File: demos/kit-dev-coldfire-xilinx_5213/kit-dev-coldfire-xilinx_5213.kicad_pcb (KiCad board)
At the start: 4 copper layers, 157.5 x 91.4 mm, 160 parts, among them J201 JACK_2P, P301 CONN_6, P302 CONN_2X2, P303 CONN_20X2, Q101 3906, SW201 SW_PUSH, SW202 SW_PUSH, U101 74AHC1G14, U102 MCF5213-LQFP100, U201 74HC125, U202 MAX202, U203 MAX202, U204 MAX202, U205 PCA82C251, U301 XCR3256-TQ144, Y101 8MHz

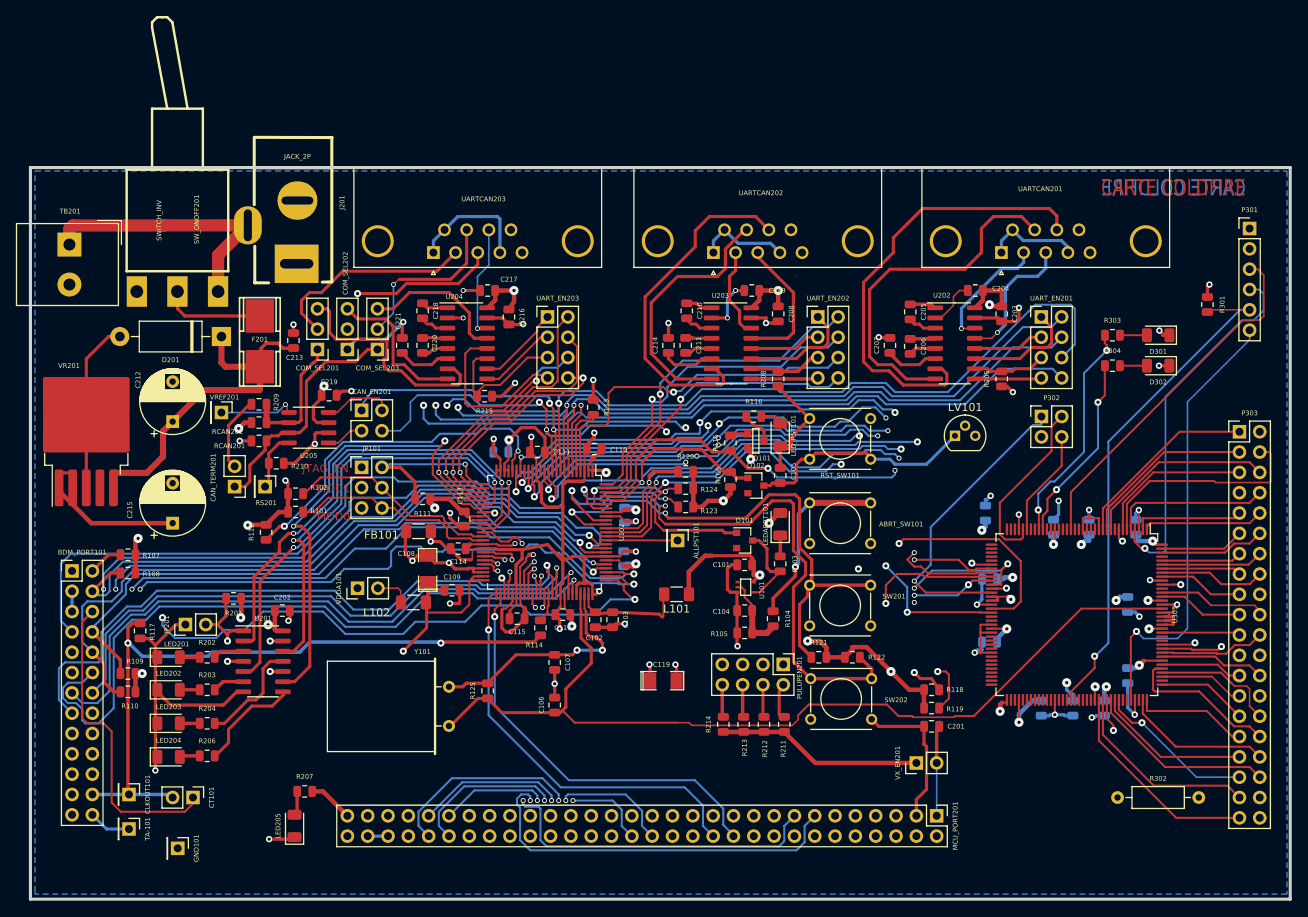
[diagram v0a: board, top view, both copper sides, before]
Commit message: feat: update kicad to 9.0.0+dfsg-1
Signed-off-by: lhdjply <lhdjply@126.com>
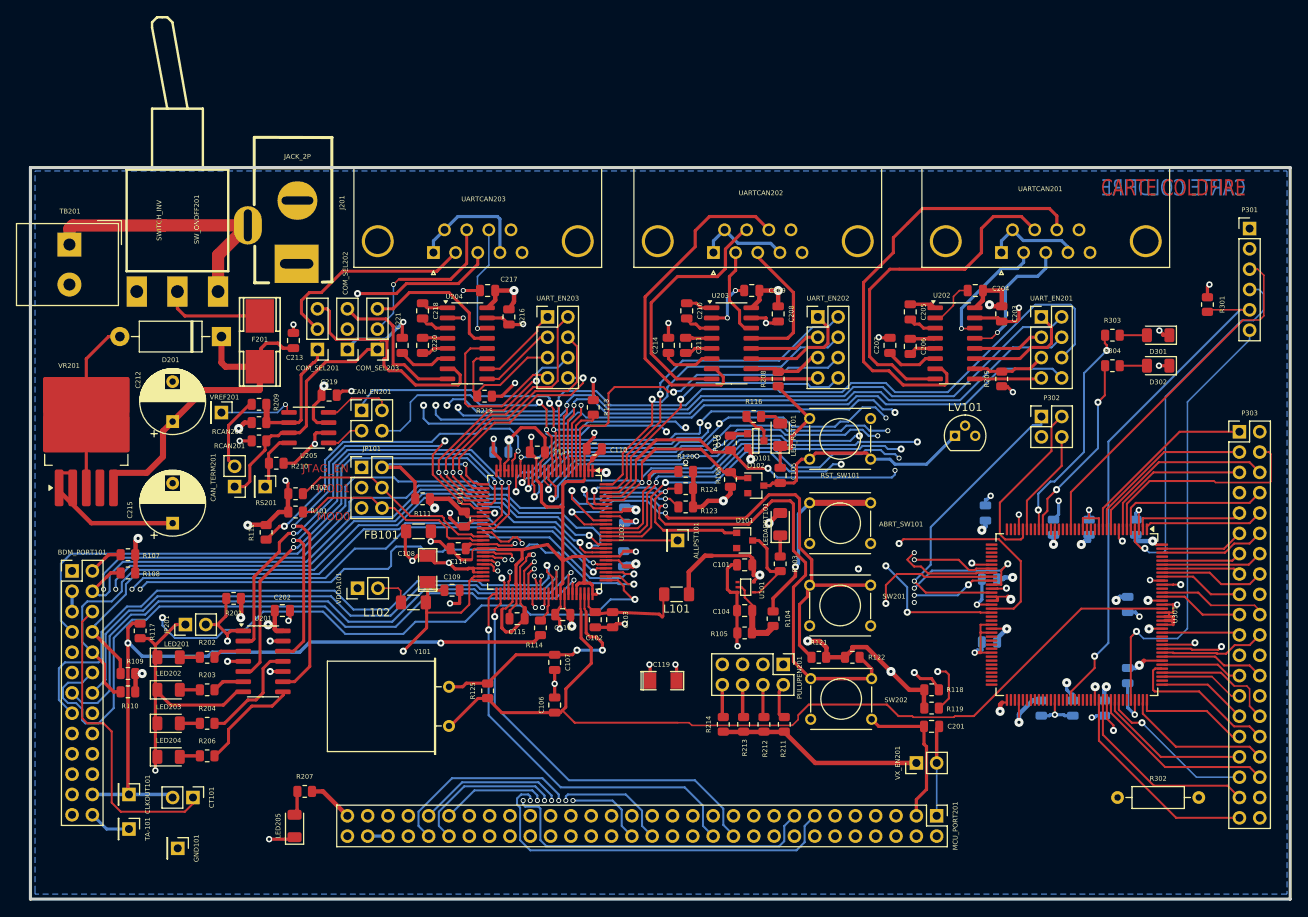
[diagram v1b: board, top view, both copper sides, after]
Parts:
- ALLPST101, CLKOUT101, GND101, RS201, TA-101, VREF201: footprint Connector_PinHeader_2.54mm:PinHeader_1x01_P2.54mm_Vertical -> kit-dev-coldfire:PinHeader_1x01_P2.54mm_Vertical
- BDM_PORT101: footprint Connector_PinHeader_2.54mm:PinHeader_2x13_P2.54mm_Vertical -> kit-dev-coldfire:PinHeader_2x13_P2.54mm_Vertical
- C101, C102, C103, C104, C105, C106, C107, C109, C110, C111, C112, C113, C114, C115, C116, C117, C118, C201, C202, C203, C204, C205, C206, C207, C208, C209, C210, C211, C213, C214, C216, C217, C218, C219, C220, C221, C301, C302, C303, C304, C305, C306, C307, C308, C309, C310, C311: footprint Capacitor_SMD:C_0805_2012Metric -> kit-dev-coldfire:C_0805_2012Metric
- C212, C215: footprint Capacitor_THT:CP_Radial_D8.0mm_P5.00mm -> kit-dev-coldfire:CP_Radial_D8.0mm_P5.00mm
- CAN_EN201, P302: footprint Connector_PinHeader_2.54mm:PinHeader_2x02_P2.54mm_Vertical -> kit-dev-coldfire:PinHeader_2x02_P2.54mm_Vertical
- CAN_TERM201, CT101, JP201, VDDA101, VX_EN201: footprint Connector_PinHeader_2.54mm:PinHeader_1x02_P2.54mm_Vertical -> kit-dev-coldfire:PinHeader_1x02_P2.54mm_Vertical
- COM_SEL201, COM_SEL202, COM_SEL203: footprint Connector_PinHeader_2.54mm:PinHeader_1x03_P2.54mm_Vertical -> kit-dev-coldfire:PinHeader_1x03_P2.54mm_Vertical
- D201: footprint Diode_THT:D_DO-15_P12.70mm_Horizontal -> kit-dev-coldfire:D_DO-15_P12.70mm_Horizontal
- D301, D302, LED201, LED202, LED203, LED204, LED205, LEDABRT101, LED_RST101: footprint LED_SMD:LED_1206_3216Metric -> kit-dev-coldfire:LED_1206_3216Metric
- FB101, L101, L102: footprint Resistor_SMD:R_1206_3216Metric_Pad1.30x1.75mm_HandSolder -> kit-dev-coldfire:R_1206_3216Metric_Pad1.30x1.75mm_HandSolder
- JP101: footprint Connector_PinHeader_2.54mm:PinHeader_2x03_P2.54mm_Vertical -> kit-dev-coldfire:PinHeader_2x03_P2.54mm_Vertical
- LV101: footprint Package_TO_SOT_THT:TO-92 -> kit-dev-coldfire:TO-92
- MCU_PORT201: footprint Connector_PinHeader_2.54mm:PinHeader_2x30_P2.54mm_Vertical -> kit-dev-coldfire:PinHeader_2x30_P2.54mm_Vertical
- P301: footprint Connector_PinHeader_2.54mm:PinHeader_1x06_P2.54mm_Vertical -> kit-dev-coldfire:PinHeader_1x06_P2.54mm_Vertical
- P303: footprint Connector_PinHeader_2.54mm:PinHeader_2x20_P2.54mm_Vertical -> kit-dev-coldfire:PinHeader_2x20_P2.54mm_Vertical
- PULUPEN201, UART_EN201, UART_EN202, UART_EN203: footprint Connector_PinHeader_2.54mm:PinHeader_2x04_P2.54mm_Vertical -> kit-dev-coldfire:PinHeader_2x04_P2.54mm_Vertical
- R101, R102, R103, R104, R105, R106, R107, R108, R109, R110, R111, R112, R113, R114, R115, R116, R117, R118, R119, R120, R121, R122, R123, R124, R125, R201, R202, R203, R204, R205, R206, R207, R208, R209, R210, R211, R212, R213, R214, R215, R301, R303, R304, RCAN201, RCAN202: footprint Resistor_SMD:R_0805_2012Metric -> kit-dev-coldfire:R_0805_2012Metric
- R302: footprint Resistor_THT:R_Axial_DIN0207_L6.3mm_D2.5mm_P10.16mm_Horizontal -> kit-dev-coldfire:R_Axial_DIN0207_L6.3mm_D2.5mm_P10.16mm_Horizontal
- TB201: footprint TerminalBlock_Altech:Altech_AK300_1x02_P5.00mm_45-Degree -> kit-dev-coldfire:Altech_AK300_1x02_P5.00mm_45-Degree
- U102: footprint Package_QFP:LQFP-100_14x14mm_P0.5mm -> kit-dev-coldfire:LQFP-100_14x14mm_P0.5mm
- U201: footprint Package_SO:SOIC-14_3.9x8.7mm_P1.27mm -> kit-dev-coldfire:SOIC-14_3.9x8.7mm_P1.27mm
- U202, U203, U204: footprint Package_SO:SOIC-16_3.9x9.9mm_P1.27mm -> kit-dev-coldfire:SOIC-16_3.9x9.9mm_P1.27mm
- U205: footprint Package_SO:SOIC-8_3.9x4.9mm_P1.27mm -> kit-dev-coldfire:SOIC-8_3.9x4.9mm_P1.27mm
- U301: footprint Package_QFP:TQFP-144_20x20mm_P0.5mm -> kit-dev-coldfire:TQFP-144_20x20mm_P0.5mm
- UARTCAN201, UARTCAN202, UARTCAN203: footprint Connector_Dsub:DSUB-9_Female_Horizontal_P2.77x2.84mm_EdgePinOffset7.70mm_Housed_MountingHolesOffset9.12mm -> kit-dev-coldfire:DSUB-9_Female_Horizontal_P2.77x2.84mm_EdgePinOffset7.70mm_Housed_MountingHolesOffset9.12mm
- VR201: footprint Package_TO_SOT_SMD:TO-263-5_TabPin3 -> kit-dev-coldfire:TO-263-5_TabPin3
- Y101: footprint Crystal:Crystal_HC18-U_Horizontal -> kit-dev-coldfire:Crystal_HC18-U_Horizontal
